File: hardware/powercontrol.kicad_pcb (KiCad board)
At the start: 2 copper layers, 45.7 x 38.1 mm, 17 parts, among them Q1 IRF9540N, Q2 IRF9540N, Q3 2N3904, SW1 SW_Push, SW2 SW_Push, U1 TL072

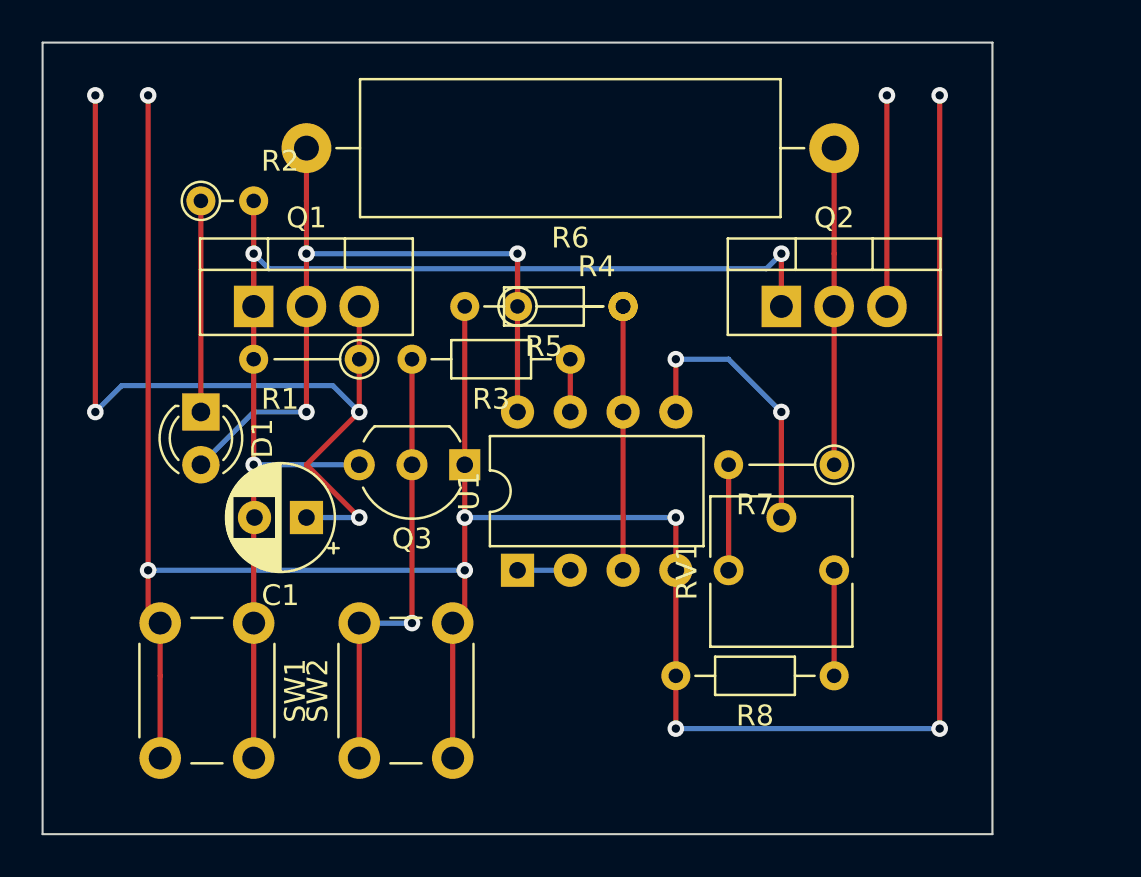
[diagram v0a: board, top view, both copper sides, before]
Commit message: V4 - Veroboard layout fixes, actually built and tested on veroboard now
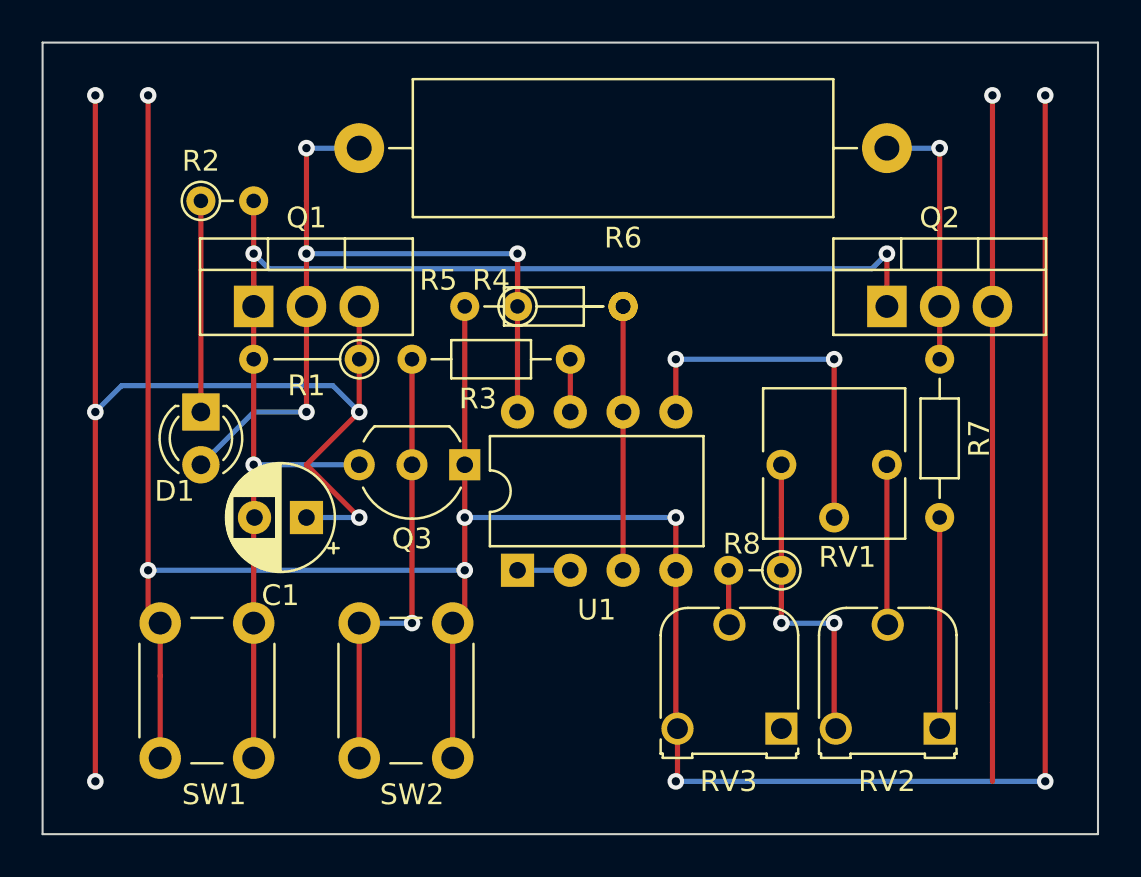
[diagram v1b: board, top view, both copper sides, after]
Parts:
- added RV2: 3K, Potentiometer_THT:Potentiometer_Runtron_RM-065_Vertical, F.Cu at (132.1, 88.9)
- added RV3: 3K, Potentiometer_THT:Potentiometer_Runtron_RM-065_Vertical, F.Cu at (124.5, 88.9)
- R6: value 1 -> 167m
- R7: footprint Resistor_THT:R_Axial_DIN0204_L3.6mm_D1.6mm_P5.08mm_Vertical -> Resistor_THT:R_Axial_DIN0204_L3.6mm_D1.6mm_P7.62mm_Horizontal
- R8: footprint Resistor_THT:R_Axial_DIN0204_L3.6mm_D1.6mm_P7.62mm_Horizontal -> Resistor_THT:R_Axial_DIN0204_L3.6mm_D1.6mm_P2.54mm_Vertical
- moved R7 7.18 mm to (132.1, 71.1), turned to 270 degrees
- moved R8 5.68 mm to (124.5, 81.3)
- moved RV1 5.68 mm to (124.5, 76.2), turned to 270 degrees
- moved Q2 5.08 mm to (129.5, 68.6)
- moved R6 2.54 mm to (129.5, 61.0)
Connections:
- R8 pad 2: GND_IN -> Net-(R8-Pad2)
- RV1 pad 3: Net-(R7-Pad2) -> Net-(RV1-Pad3)
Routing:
- net V_OUT: track 10.2 -> 33.0 mm
- net V_IN: track 43.8 -> 61.6 mm, vias 4 -> 5
- net GND_IN: track 132.9 -> 143.1 mm
- net Net-(R8-Pad1): track 5.08 -> 15.2 mm, vias 0 -> 2
- net Net-(RV1-Pad3): track 0.00 -> 7.66 mm
- net Net-(R7-Pad2): track 5.08 -> 10.2 mm
- net Net-(C1-Pad2): track 63.0 -> 68.1 mm
- net Net-(RV1-Pad2): track 13.8 -> 17.8 mm
- net Net-(R8-Pad2): track 0.00 -> 2.58 mm
- net Net-(D1-Pad2): track 39.2 -> 41.7 mm, vias 3 -> 4
- net Net-(Q2-Pad2): track 15.2 -> 12.7 mm, vias 0 -> 1
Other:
- board size 45.7 x 38.1 mm -> 50.8 x 38.1 mm
